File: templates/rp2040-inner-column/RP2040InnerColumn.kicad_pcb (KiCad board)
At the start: 2 copper layers, 19.6 x 41.6 mm, 35 parts, among them J1 Connector, USB-TYPE-C-16P, SW1 BOOT, SW2 RESET, U1 RP2040, U3 W25Q128, U4 SRV05-4, U5 AP2112K-3.3, X1 ABM8-272-T3

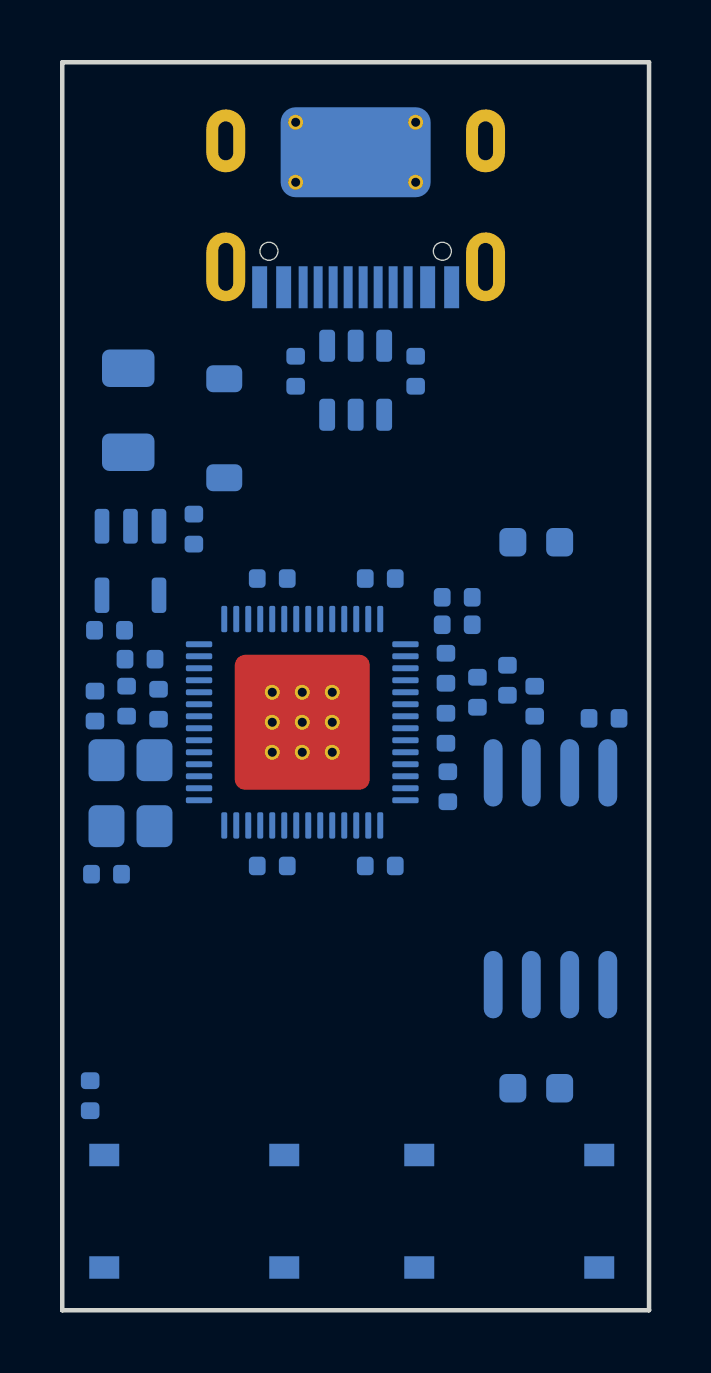
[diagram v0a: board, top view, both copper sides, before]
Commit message: fix(templates): re-place rp2040 module at 45 degrees so it can be routed
The first placement passed DRC but could not be routed: parts sat 0.26 mm
apart and crowded the RP2040 pins. The module is re-placed with routing room
and checked by autorouting instead of DRC alone.

- Routable: the only variant Freerouting routed 100% on 2 layers, confirmed
  in KiCad DRC at 0.15 mm with every signal and power net connected
- Room to route: 0.6 mm minimum between parts, 1.6 mm fanout ring at U1
- Short GPIO escapes: RP2040 at 45 degrees faces its GPIO sides toward the
  key area, flash turned to face the QSPI pins
- Fine-pitch rule: .kicad_dru allows 0.15 mm clearance at U1 and J1 only
- Net classes restored: Power3.3V, Power5V and USB with their patterns
- Placer handles rotated parts; JLC marker now always lands on the board
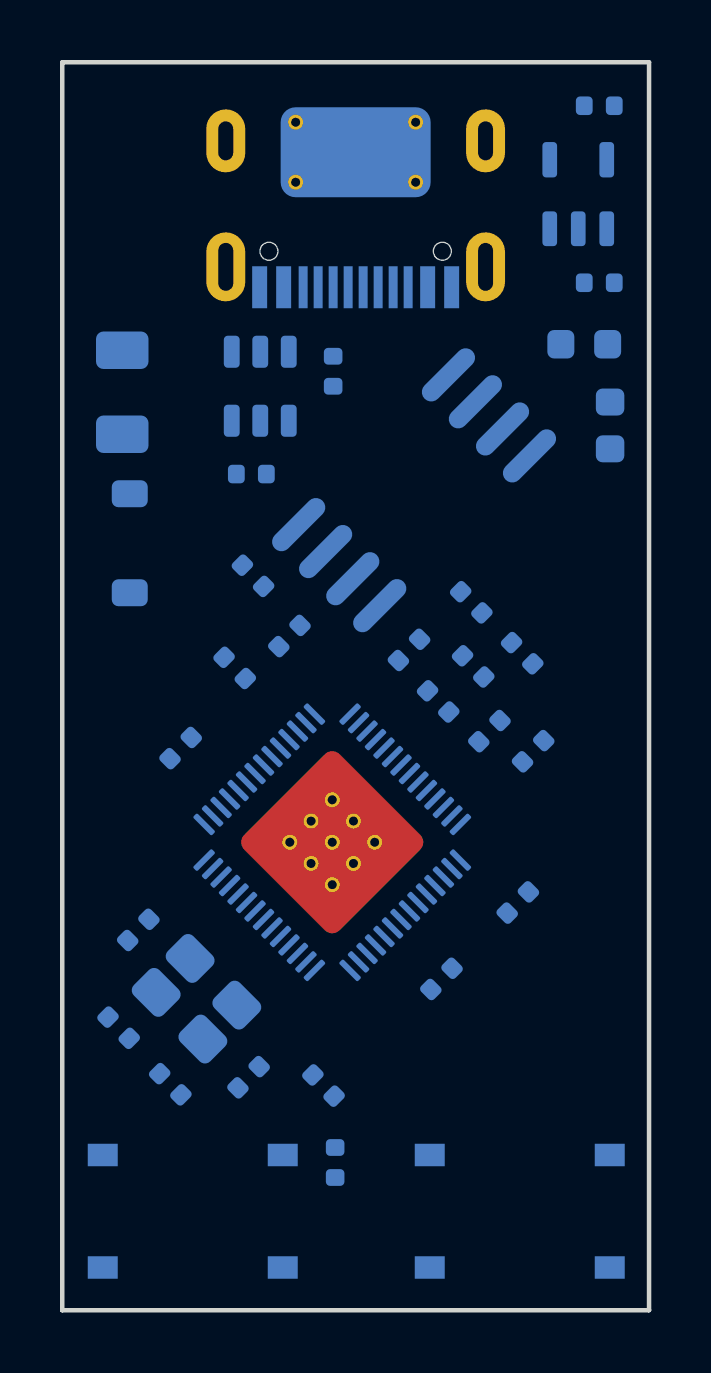
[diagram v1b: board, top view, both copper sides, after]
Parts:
- moved C19 23.9 mm to (17.9, 1.45)
- moved C9 22.2 mm to (18.3, 12.1), turned to 90 degrees
- moved U5 19.3 mm to (17.2, 4.40), turned to 180 degrees
- moved C20 15.8 mm to (17.9, 7.35), turned to 180 degrees
- moved C12 15.5 mm to (8.71, 34.1), turned to 135 degrees
- moved U3 13.7 mm to (11.7, 14.3), turned to -45 degrees
- moved R2 12.9 mm to (3.60, 34.1), turned to 135 degrees
- moved C3 12.6 mm to (6.36, 17.1), turned to 135 degrees
- moved C1 10.9 mm to (1.88, 32.2), turned to 135 degrees
- moved R4 8.46 mm to (9.10, 36.7)
- moved C4 8.26 mm to (6.21, 33.8), turned to 45 degrees
- moved C5 7.55 mm to (2.54, 28.9), turned to 45 degrees
- moved X1 7.20 mm to (4.47, 31.2), turned to 135 degrees
- moved C18 6.79 mm to (17.4, 9.40)
- moved C11 6.78 mm to (12.6, 30.6), turned to 45 degrees
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
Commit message: refactor(templates): split rp2040 module into two groups, drop outline
The module is pasted into an existing keyboard board, so it no longer carries
its own Edge.Cuts. Following ScottoModules, the parts now sit in two groups
that move as units on the host board.

- Paste-ready: no board outline to delete after copying into a keyboard
- Two modules: "USB and power" (connector, ESD, fuse, diode, regulator) and
  "RP2040" (MCU, flash, crystal, decoupling, BOOT/RESET, JLC marker)
- Same placement as before, so the routability check still applies
- README and template description explain the groups and the expected
  invalid_outline DRC item
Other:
- board outline removed

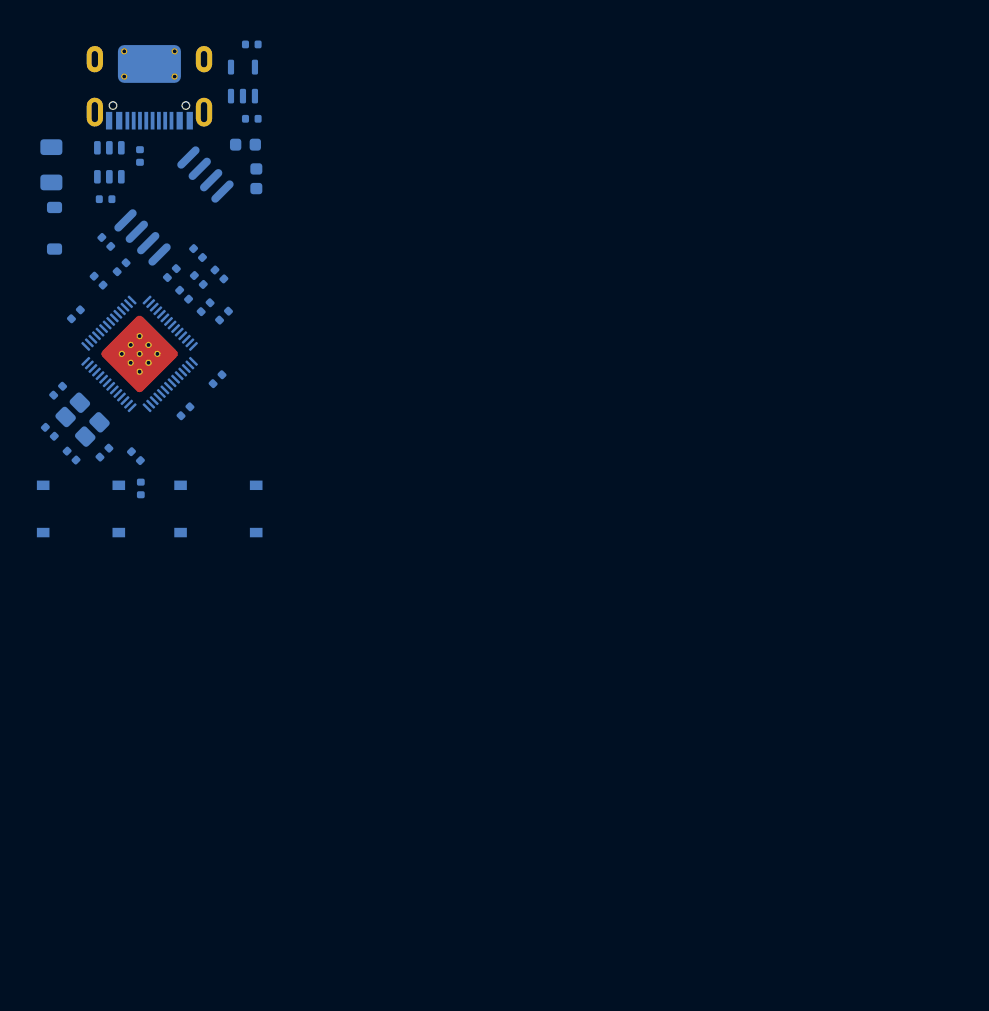
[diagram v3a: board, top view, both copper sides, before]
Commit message: feat(templates): route the rp2040 module on 2 layers
The 135 degree module is now fully routed. KiCad Routing Tools did the QFN
fanout, GND pour and first pass on a test board; the rest was finished by
hand in KiCad 10 and copied onto the template.

- Ready to wire: every GPIO runs out to the strip's left or bottom edge
- Checked: 0 schematic parity issues, no clearance, via or hole errors
- Buildable at JLCPCB standard 2-layer limits (0.127 mm clearance and
  track, 0.45/0.2 mm vias); the 0.15 mm fine-pitch rule file is dropped
  as redundant
- Repeatable copy: scripts/transfer_module_routing.py cuts GPIOs at the
  strip edge and leaves the test pads behind
- README lists the known leftovers: +3.3V, RUN and +1V1 detour up to
  2.2 mm past the strip, and one GND pour piece that rejoins through the
  host board's pour
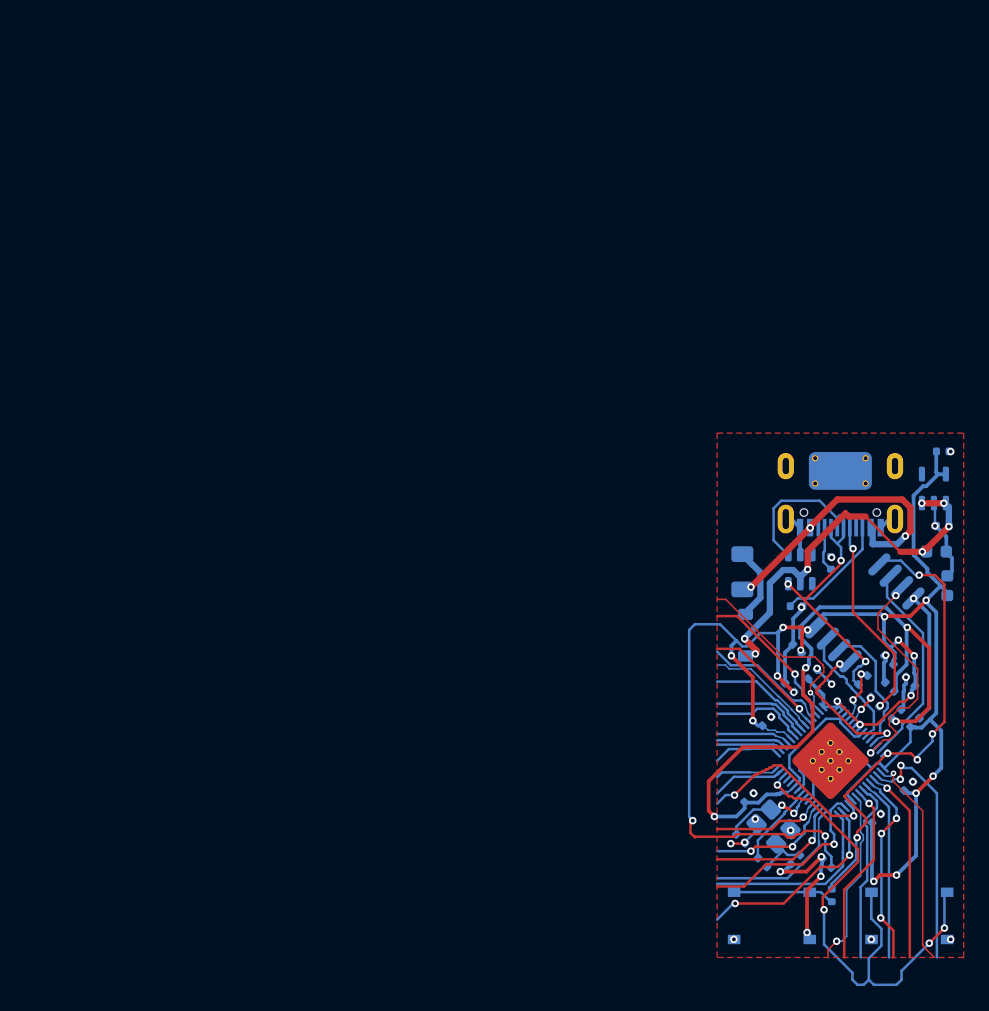
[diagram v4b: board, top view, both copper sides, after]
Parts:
- moved C1 63.6 mm to (56.7, 64.5)
- moved C10 63.6 mm to (70.0, 60.3)
- moved C12 63.6 mm to (63.5, 66.4)
- moved C15 63.6 mm to (70.1, 52.0)
- moved C17 63.6 mm to (68.4, 50.3)
- moved C5 63.6 mm to (57.4, 61.2)
- moved C6 63.6 mm to (69.1, 54.6)
- moved C8 63.6 mm to (68.5, 52.4)
- moved C9 63.6 mm to (73.1, 44.4)
- moved J1 63.6 mm to (64.6, 37.3)
- moved R4 63.6 mm to (63.9, 69.0)
- moved R7 63.6 mm to (67.3, 53.6)
- moved R8 63.6 mm to (66.4, 51.9)
- moved SW1 63.6 mm to (59.2, 70.6)
- moved SW2 63.6 mm to (70.1, 70.6)
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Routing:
- net +3.3V: track 0.00 -> 164.0 mm, vias 0 -> 20
- net +1V1: track 0.00 -> 66.9 mm, vias 0 -> 4
- net GND: track 0.00 -> 56.9 mm, vias 0 -> 24
- net RUN: track 0.00 -> 42.5 mm, vias 0 -> 4
- net SS: track 0.00 -> 37.2 mm, vias 0 -> 5
- net +5V: track 0.00 -> 32.4 mm, vias 0 -> 7
- net D_USB_P: track 0.00 -> 28.8 mm, vias 0 -> 2
- net VBUS: track 0.00 -> 23.3 mm, vias 0 -> 3
- net GP1: track 0.00 -> 19.9 mm, vias 0 -> 2
- net D_USB_N: track 0.00 -> 19.9 mm, vias 0 -> 3
- net SD2: track 0.00 -> 18.7 mm, vias 0 -> 2
- net GP0: track 0.00 -> 16.7 mm, vias 0 -> 1
- net SD1: track 0.00 -> 16.5 mm
- net GP10: track 0.00 -> 16.3 mm, vias 0 -> 2
- net GP3: track 0.00 -> 15.7 mm, vias 0 -> 3
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- added copper zone on F.Cu, net GND
